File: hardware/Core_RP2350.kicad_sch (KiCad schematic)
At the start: 66 parts, among them U1 RP2350B-QFN80, U2 LM4040A30IDBZR, U3 W25Q128JVS, U4 W25Q128JVS, U5 W25Q128JVS

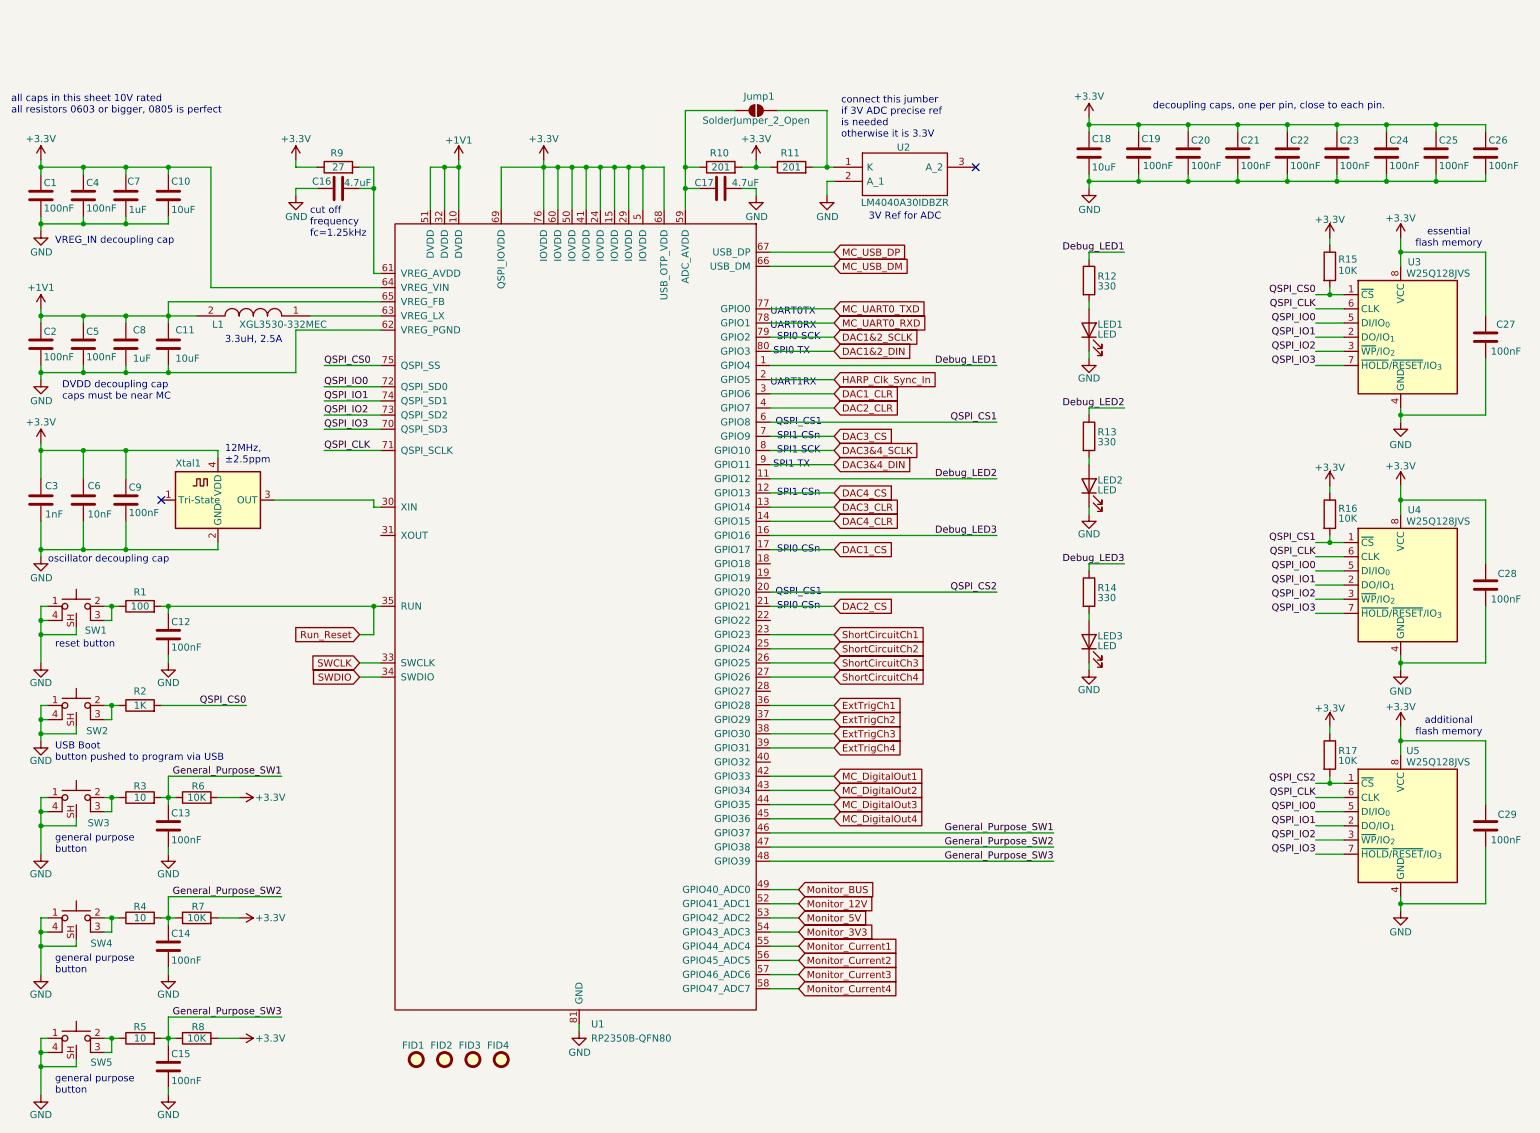
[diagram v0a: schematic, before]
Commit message: Added caps voltage rating + block diagram
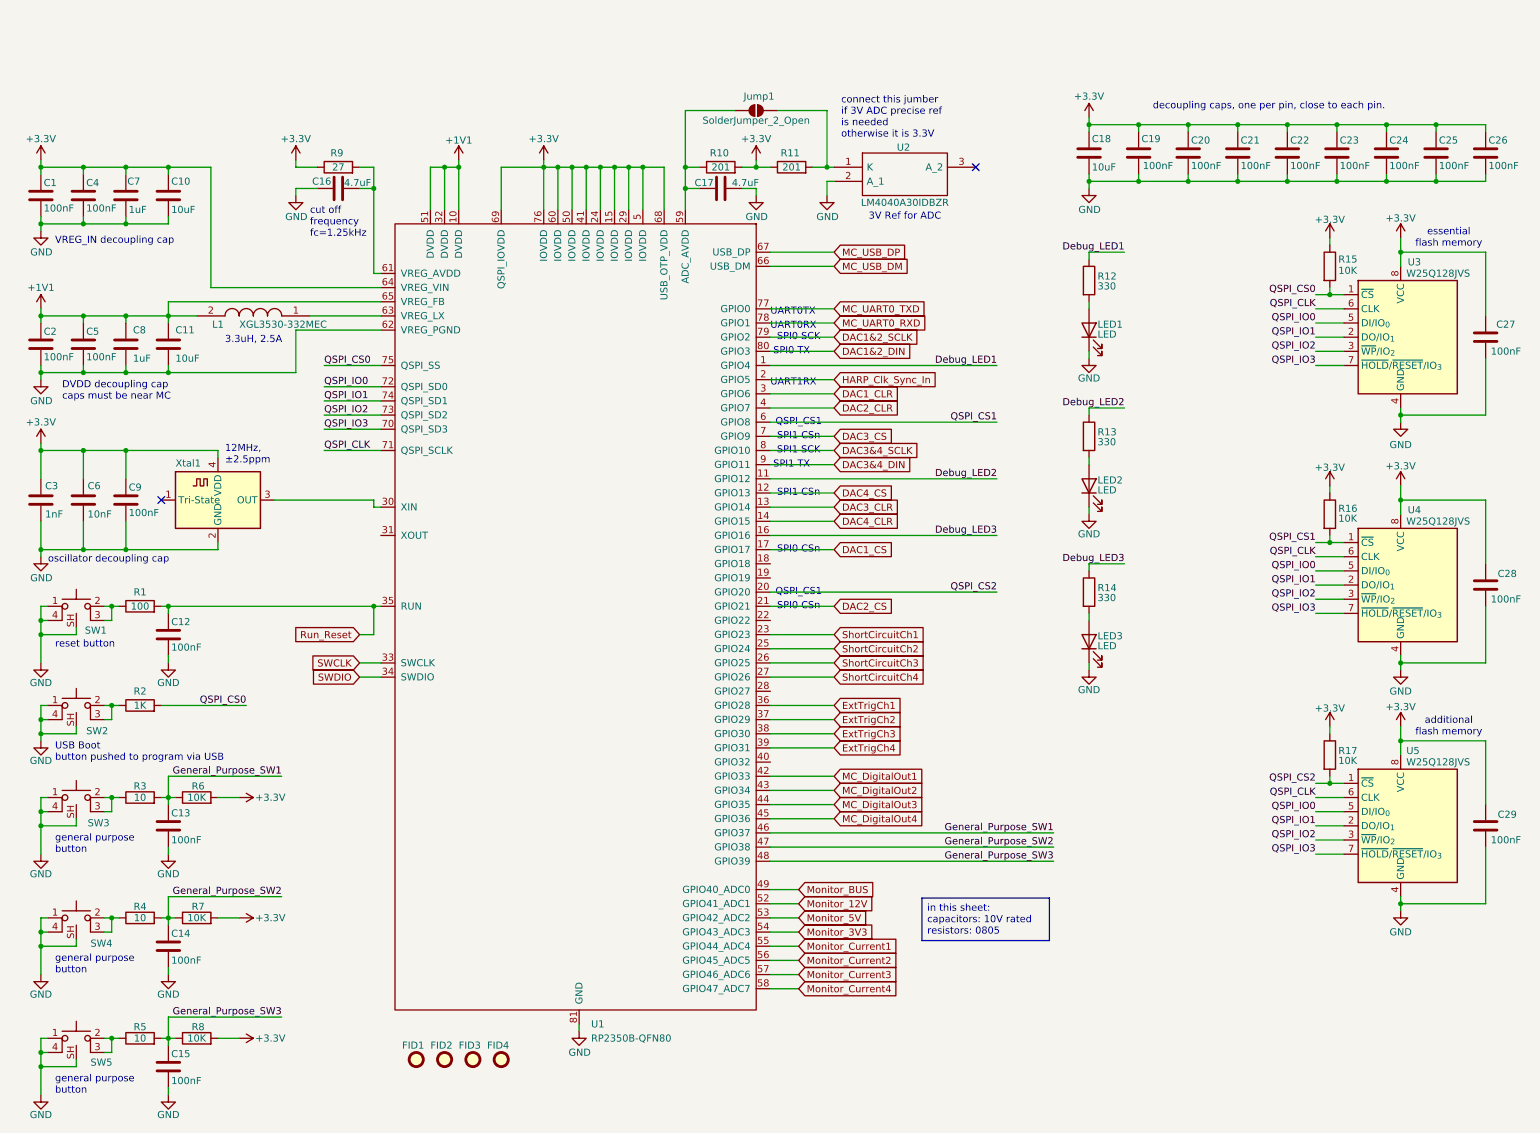
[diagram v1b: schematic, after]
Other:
- note removed: "all caps in this sheet 10V rated all resistors 0603 or bigger, 0805 is perfect"
- title: Multi Channel HARP DAC -> harp device quad dac

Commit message: The footprint assigning and reviewing have started.
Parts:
- C1, C10, C11, C12, C13, C14, C15, C16, C17, C18, C19, C2, C20, C21, C22, C23, C24, C25, C26, C27, C28, C29, C3, C4, C5, C6, C7, C8, C9: symbol Device:C -> harp.device.quad.dac:C
- FID1, FID2, FID3, FID4: symbol Mechanical:Fiducial -> harp.device.quad.dac:Fiducial
- Jump1: symbol Jumper:SolderJumper_2_Open -> harp.device.quad.dac:SolderJumper_2_Open
- L1: symbol XGL3530-332MEC:XGL3530-332MEC -> harp.device.quad.dac:XGL3530-332MEC
- LED1, LED2, LED3: symbol Device:LED -> harp.device.quad.dac:LED
- R1, R10, R11, R12, R13, R14, R15, R16, R17, R2, R3, R4, R5, R6, R7, R8, R9: symbol Device:R -> harp.device.quad.dac:R
- SW1, SW2, SW3, SW4, SW5: symbol kicad_component_library:SW_Push_with_gnd -> harp.device.quad.dac:SW_Push_with_gnd
- U1: footprint (none) -> harp.device.quad.dac.kicad:RP2350B_QFN-80_EP_10.573x10.573_Pitch0.4mm; symbol rp2350b-qfn80:RP2350B-QFN80 -> harp.device.quad.dac:RP2350B-QFN80
- U2: symbol LM4040A30IDBZR:LM4040A30IDBZR -> harp.device.quad.dac:LM4040A30IDBZR
- U3, U4, U5: symbol Memory_Flash:W25Q128JVS -> harp.device.quad.dac:W25Q128JVS_1
- Xtal1: footprint Crystal:Crystal_SMD_2016-4Pin_2.0x1.6mm -> harp.device.quad.dac.kicad:Crystal_SMD_2016-4Pin_2.0x1.6mm; symbol kicad_component_library:ECS-TXO-2016 -> harp.device.quad.dac:ECS-TXO-2016

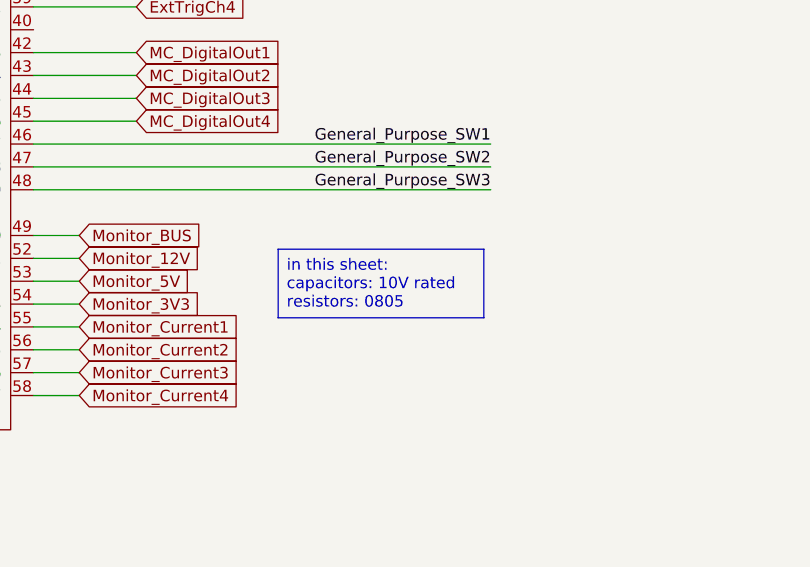
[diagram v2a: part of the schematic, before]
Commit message: Modified notes about caps and resistors
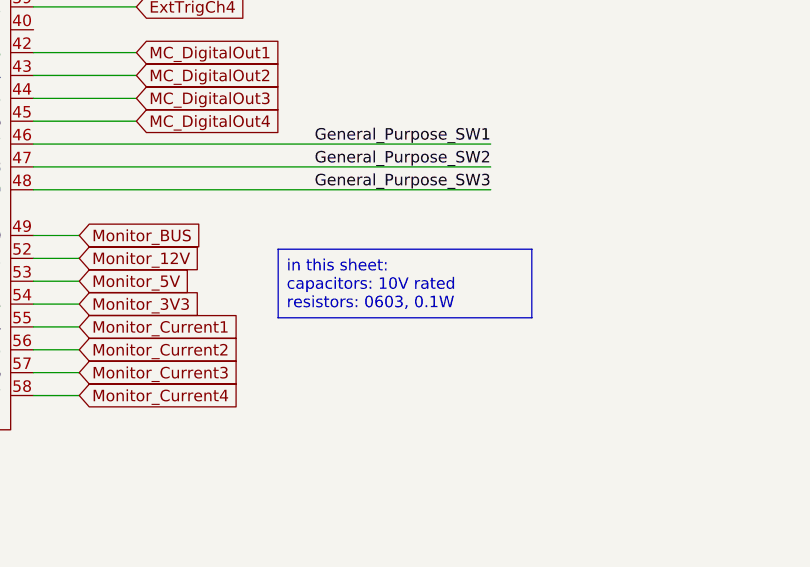
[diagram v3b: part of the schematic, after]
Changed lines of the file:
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@@
 		)
 	)
-	(text_box "in this sheet:\ncapacitors: 10V rated\nresistors: 0805"
+	(text_box "in this sheet:\ncapacitors: 10V rated\nresistors: 0603, 0.1W"
 		(exclude_from_sim no)
 		(at 177.038 157.734 0)
-		(size 22.86 7.62)
+		(size 28.194 7.62)
 		(margins 0.9525 0.9525 0.9525 0.9525)
 		(stroke
@@
 				(size 1.27 1.27)
 			)
-			(justify left top)
+			(justify left)
 		)
 	)

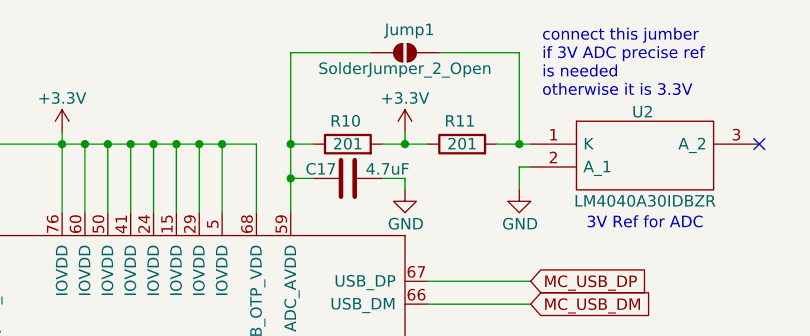
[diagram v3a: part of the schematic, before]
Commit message: Updating some footprints
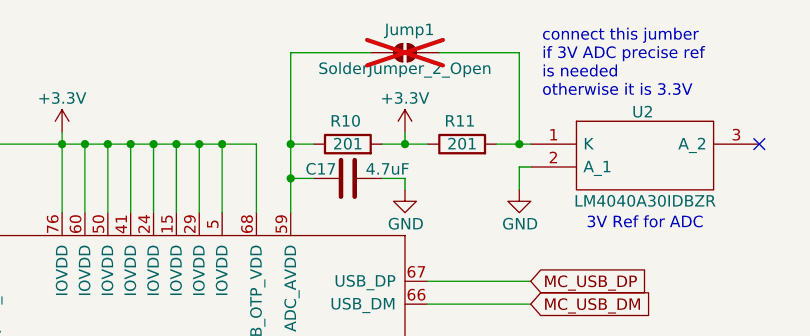
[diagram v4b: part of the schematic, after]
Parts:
- C1, C12, C13, C14, C15, C19, C2, C20, C21, C22, C23, C24, C25, C26, C27, C28, C29, C3, C4, C5, C6, C7, C8, C9: footprint Capacitor_SMD:C_0402_1005Metric -> Capacitor_SMD:C_0603_1608Metric; symbol harp.device.quad.dac:C -> harp.device.quad.dac:C_0603
- C10, C11, C16, C17, C18: footprint Capacitor_SMD:C_0805_2012Metric -> Capacitor_SMD:C_0603_1608Metric; symbol harp.device.quad.dac:C -> harp.device.quad.dac:C_0603
- FID1, FID2, FID3, FID4: footprint Fiducial:Fiducial_0.5mm_Mask1mm -> harp.device.quad.dac.kicad:Fiducial_0.5mm_Mask1mm; now left out of the parts list
- Jump1: footprint (none) -> harp.device.quad.dac.kicad:R_0603_1608Metric_Pad0.98x0.95mm_HandSolder; now not fitted; now left out of the parts list
- L1: footprint XGL3530332MEC -> harp.device.quad.dac.kicad:XGL3530332MEC
- LED1, LED2, LED3: footprint LED_SMD:LED_0603_1608Metric_Pad1.05x0.95mm_HandSolder -> harp.device.quad.dac.kicad:LED_0603_1608Metric_Pad1.05x0.95mm_HandSolder; MFN (none) -> SunLED; MPN (none) -> XZCDGK53W-1VF
- R1, R10, R11, R12, R13, R14, R15, R16, R17, R2, R3, R4, R5, R6, R7, R8, R9: footprint Resistor_SMD:R_0402_1005Metric -> Resistor_SMD:R_0603_1608Metric; symbol harp.device.quad.dac:R -> harp.device.quad.dac:R_0603
- SW1, SW2, SW3, SW4, SW5: footprint kicad_component_library:SW_Push_1P1T-SH_NO_Vertical_Wuerth_WS-TASV -> harp.device.quad.dac.kicad:SW_Push_1P1T-SH_NO_Vertical_Wuerth_WS-TASV; Alternate https://www.digikey.com/en/products/detail/w%C3%BCrth-elekt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 -> (none); Link https://www.digikey.com/en/products/detail/w%C3%BCrth-elekt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 -> (none); MFN (none) -> Würth Elektronik; MPN (none) -> 435451019820; Manufacturer Würth Elektronik -> (none); Manufacturer Number 435451019820 -> (none); Notes aqueous washable -> (none); Supplier Link (none) -> https://www.digikey.com/en/products/detail/w%C3%BCrth-elekt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
- U1: MFN (none) -> Raspberry Pi; MPN (none) -> SC1510-A4; Supplier Link (none) -> https://www.digikey.com/en/products/detail/raspberry-pi/SC1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
- U3, U4, U5: footprint Package_SO:SOIC-8_5.3x5.3mm_P1.27mm -> harp.device.quad.dac.kicad:SOIC-8_5.3x5.3mm_P1.27mm; symbol harp.device.quad.dac:W25Q128JVS_1 -> harp.device.quad.dac:W25Q128JVS
- Xtal1: MFN (none) -> ECS Inc.; MPN (none) -> ECS-TXO-2016-33-120-TR; Supplier Link (none) -> https://www.digikey.com/en/products/detail/ecs-inc/ECS-TXO-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

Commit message: The layout design has begun.
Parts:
- added J19: Conn_01x02, Connector_PinHeader_2.54mm:PinHeader_1x02_P2.54mm_Vertical, symbol harp.device.quad.dac:Conn_01x02
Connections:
- net at C17.1, Jump1.1 (A), R10.1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: now also J19.1 (Pin_1)
- net at Jump1.2 (B), R11.2, U2.1 (K): now also J19.2 (Pin_2)
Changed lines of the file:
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@@
 	)
 	(junction
+		(at 134.62 16.51)
+		(diameter 0)
+		(color 0 0 0 0)
+	)
+	(junction
 		(at 93.98 26.67)
 		(diameter 0)
@@
 	)
 	(junction
+		(at 160.02 16.51)
+		(diameter 0)
+		(color 0 0 0 0)
+	)
+	(junction
 		(at 19.05 185.42)
 		(diameter 0)
@@
 	(wire
 		(pts
+			(xy 160.02 6.35) (xy 160.02 16.51)
+		)
+		(stroke
+			(width 0)
+			(type default)
+		)
+	)
+	(wire
+		(pts
+			(xy 134.62 6.35) (xy 134.62 16.51)
+		)
+		(stroke
+			(width 0)
+			(type default)
+		)
+	)
+	(wire
+		(pts
 			(xy 19.05 128.27) (xy 19.05 125.73)
 		)
@@
 	(wire
 		(pts
+			(xy 148.59 6.35) (xy 160.02 6.35)
+		)
+		(stroke
+			(width 0)
+			(type default)
+		)
+	)
+	(wire
+		(pts
 			(xy 149.86 171.45) (xy 154.94 171.45)
 		)
@@
 	(wire
 		(pts
+			(xy 146.05 6.35) (xy 134.62 6.35)
+		)
+		(stroke
+			(width 0)
+			(type default)
+		)
+	)
+	(wire
+		(pts
 			(xy 19.05 128.27) (xy 25.4 128.27)
 		)
@@
 					(unit 1)
 				)
+			)
+		)
+	)
+	(symbol
+		(lib_id "harp.device.quad.dac:Conn_01x02")
+		(at 146.05 1.27 90)
+		(unit 1)
+		(exclude_from_sim no)
+		(in_bom yes)
+		(on_board yes)
+		(dnp no)
+		(fields_autoplaced yes)
+		(property "Reference" "J19"
+			(at 151.13 -0.0001 90)
+			(effects
+				(font
+					(size 1.27 1.27)
+				)
+				(justify right)
+			)
+		)
+		(property "Value" "Conn_01x02"
+			(at 151.13 2.5399 90)
+			(effects
+				(font
+					(size 1.27 1.27)
+				)
+				(justify right)
+			)
+		)
+		(property "Footprint" "Connector_PinHeader_2.54mm:PinHeader_1x02_P2.54mm_Vertical"
+			(at 146.05 1.27 0)
+			(effects
+				(font
+					(size 1.27 1.27)
+				)
+				(hide yes)
+			)
+		)
+		(property "Datasheet" "~"
+			(at 146.05 1.27 0)
+			(effects
+				(font
+					(size 1.27 1.27)
+				)
+				(hide yes)
+			)
+		)
+		(property "Description" "Generic connector, single row, 01x02, script generated (kicad-library-utils/schlib/autogen/connector/)"
+			(at 146.05 1.27 0)
+			(effects
+				(font
+					(size 1.27 1.27)
+				)
+				(hide yes)
+			)
+		)
+		(pin "2"
+		)
+		(pin "1"
+		)
+		(instances
+			(project ""
+				(path "/6b47c519-21c4-43bd-9777-b273999e4447/5973743b-c3fc-4963-acef-26c8fa426708"
+					(reference "J19")
+					(unit 1)
+				)

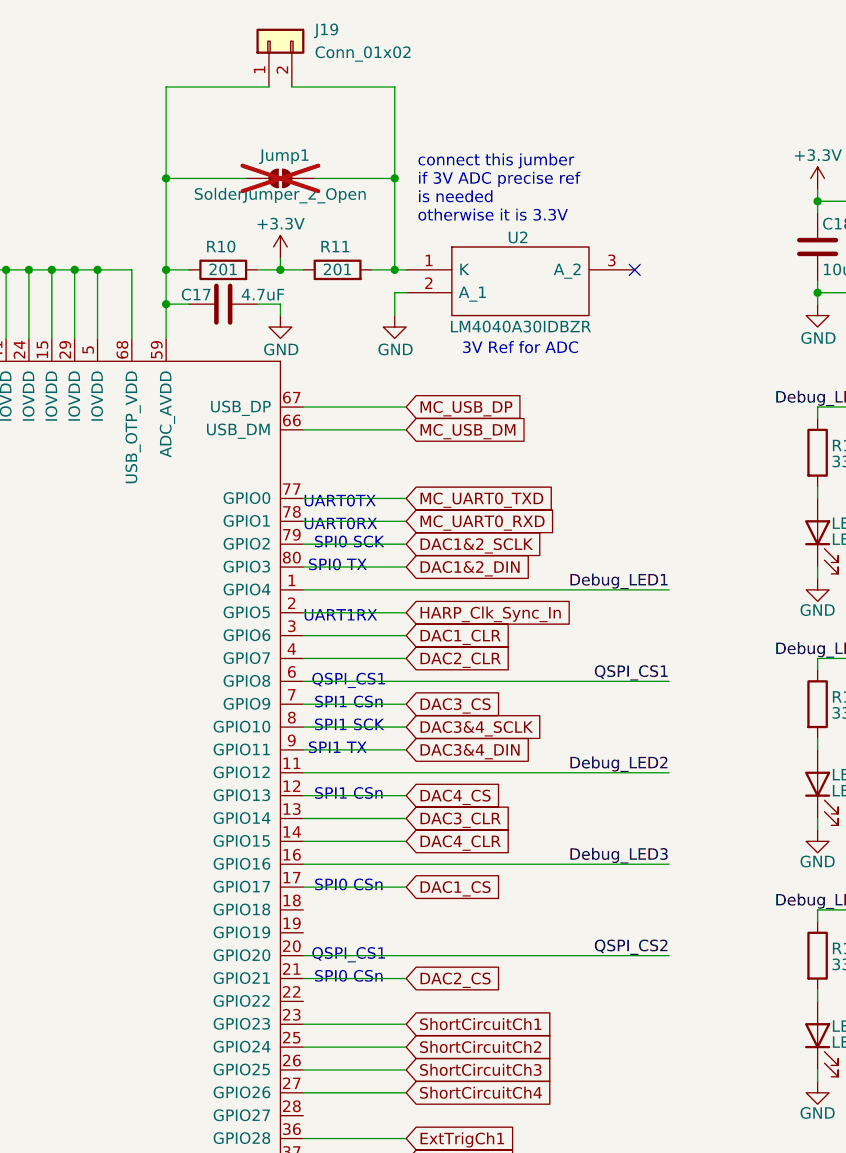
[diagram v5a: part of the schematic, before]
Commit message: Jumpers and interstages connections + added zeners to supply sections + justified text
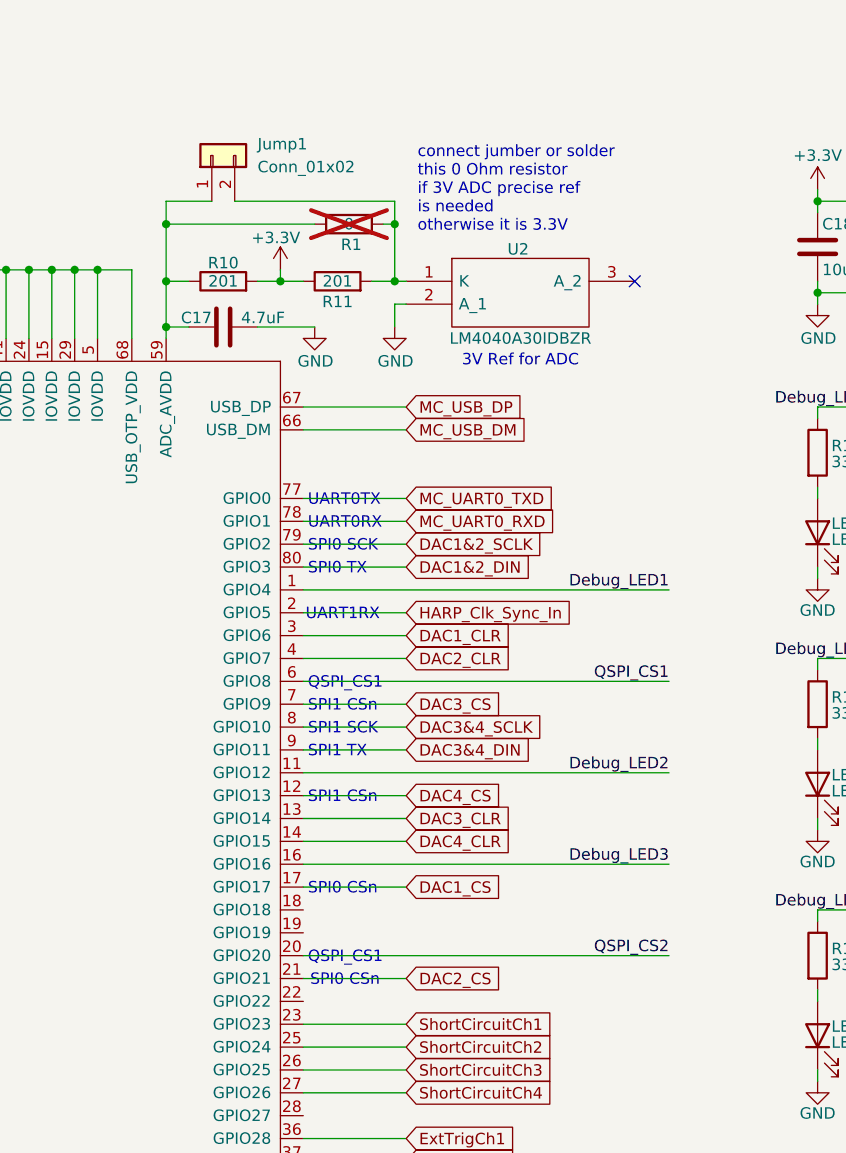
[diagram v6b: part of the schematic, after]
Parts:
- removed J19: Conn_01x02, Connector_PinHeader_2.54mm:PinHeader_1x02_P2.54mm_Vertical, symbol harp.device.quad.dac:Conn_01x02
- removed Jump1: SolderJumper_2_Open, harp.device.quad.dac.kicad:R_0603_1608Metric_Pad0.98x0.95mm_HandSolder, symbol harp.device.quad.dac:SolderJumper_2_Open
- added Jump1: Conn_01x02, Connector_PinHeader_2.54mm:PinHeader_1x02_P2.54mm_Vertical, symbol harp.device.quad.dac:Conn_01x02
- added R1: 0, Resistor_SMD:R_0603_1608Metric, symbol harp.device.quad.dac:R_0603
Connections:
- net at C17.1, R10.1, U1.59 (ADC_AVDD): now also Jump1.1 (Pin_1), R1.1
- net at R11.2, U2.1 (K): now also Jump1.2 (Pin_2), R1.2
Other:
- note added: "connect jumber or solder this 0 Ohm resistor if 3V ADC precise ref is needed otherwise it is 3.3V"
- note removed: "connect this jumber if 3V ADC precise ref is needed otherwise it is 3.3V"
- moved on the sheet: C17, R10, R11, U2
